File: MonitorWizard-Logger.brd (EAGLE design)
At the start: 120 x 80 mm, 28 parts, among them SW1 ACTION, U1 DHT22, U2 RFM69HW, U3 LTC3531, U4-NRF24L01 NRF24L01+-PCB-AERIAL, U6 ATMEGA328P-PU, X3 POWERSUPPLY_DC21MMX, Y3 32.768kHz

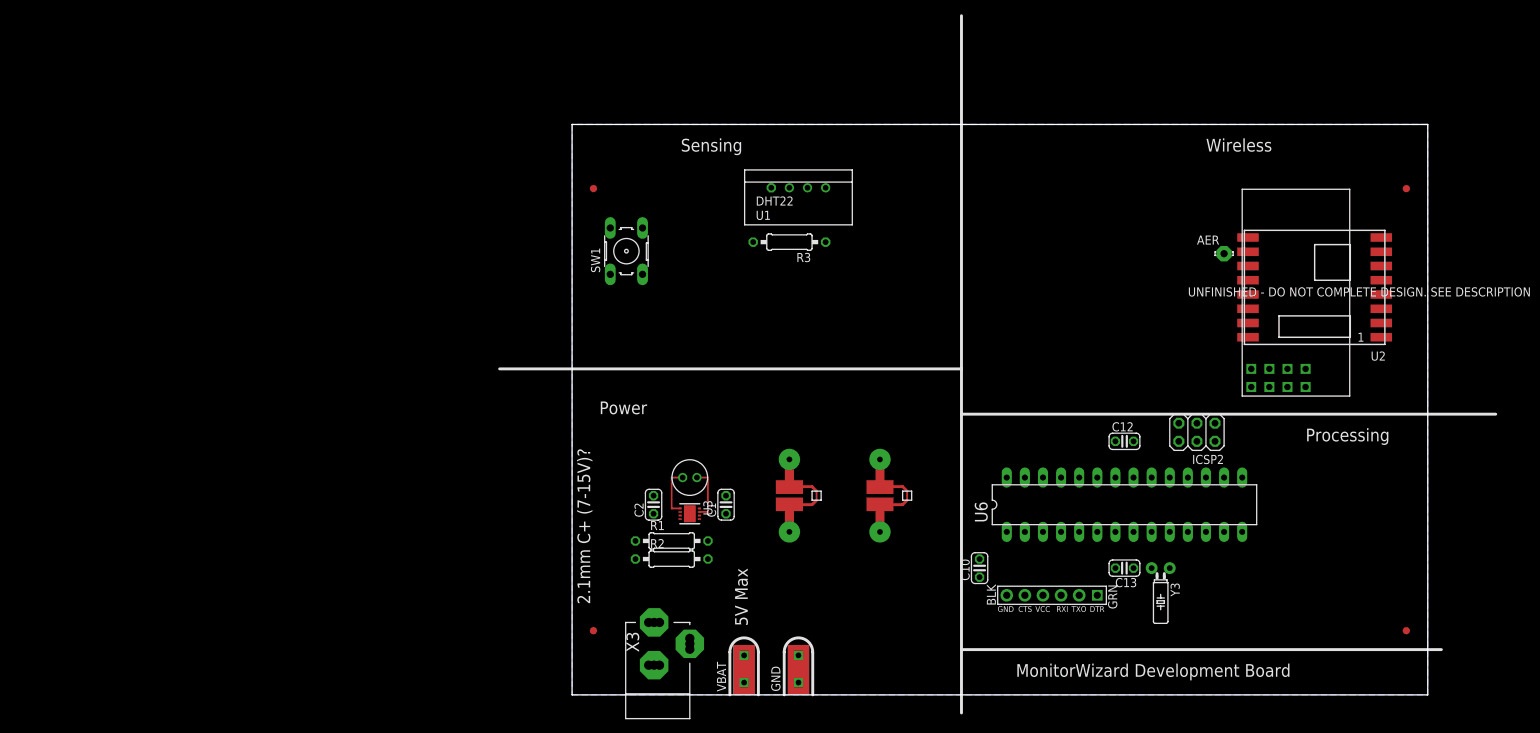
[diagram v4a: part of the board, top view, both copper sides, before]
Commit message: Add SD card, battery box. Nearly finished - just have to connect SD and lay out.
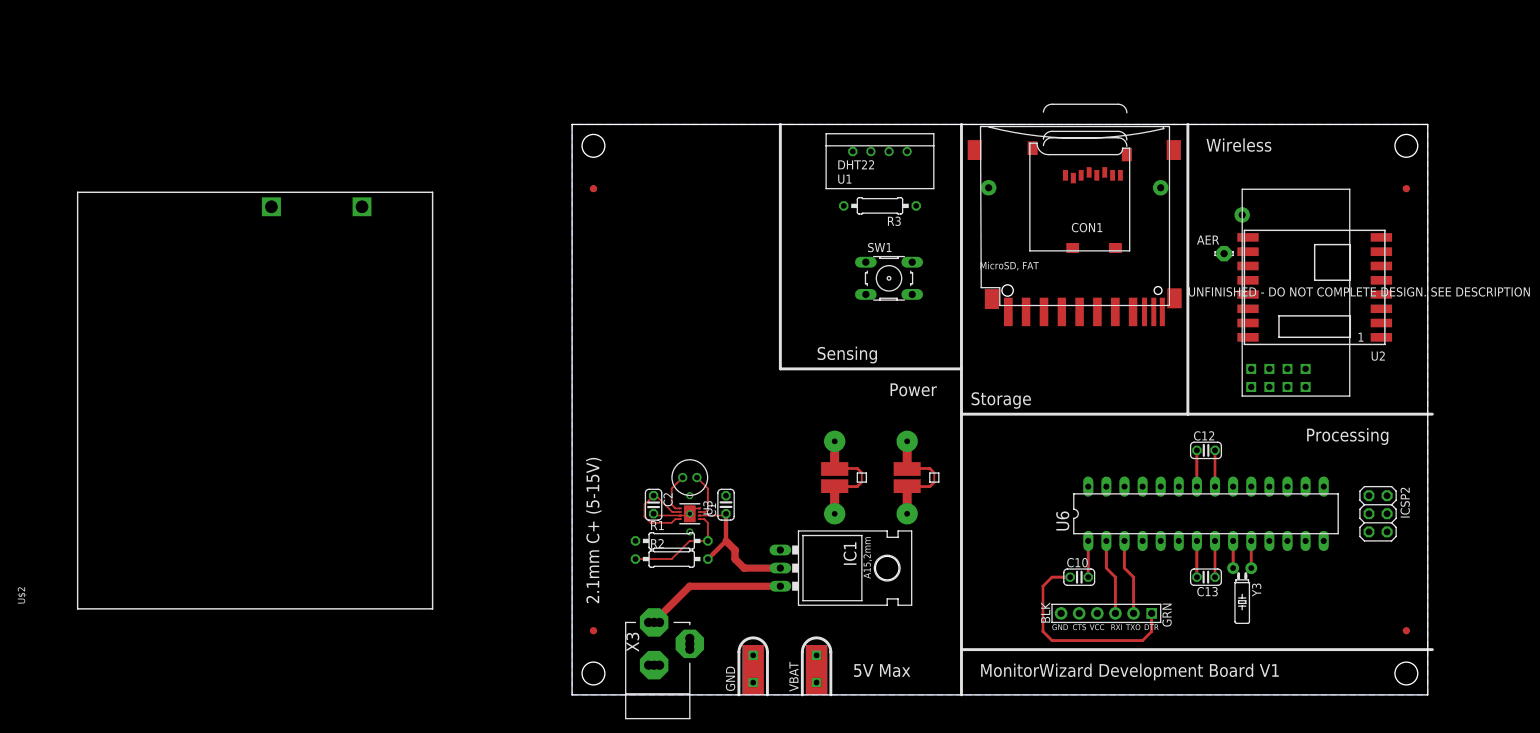
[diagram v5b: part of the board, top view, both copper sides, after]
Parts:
- added CON1: MICROSD, adafruit:MICROSD
- added IC1: LD117AV33, v-reg:TO220L1
- added U$1: SDMMC06132, adafruit:06132
- added U$2: 2464, keystone:2464
- moved SW1 37.0 mm to (44.5, 58.4), turned to 0 degrees
- moved ICSP2 27.9 mm to (113.0, 25.4), turned to 270 degrees
- moved C10 14.0 mm to (71.1, 16.5), turned to 0 degrees
- moved R3 13.7 mm to (43.2, 68.6)
- moved U1 12.5 mm to (43.2, 76.2)
- moved C12 11.5 mm to (88.9, 34.3)
- moved C13 11.5 mm to (88.9, 16.5)
- moved U6 11.5 mm to (88.9, 25.4)
- moved Y3 11.4 mm to (94.0, 17.8)
- moved VBAT 10.2 mm to (34.3, 0.00)
- moved JP1 8.03 mm to (74.9, 11.4)
- moved SENSOR_CURRENT 6.84 mm to (36.8, 30.5)
- moved GND 6.35 mm to (25.4, 0.00)
- moved RF_CURRENT 4.58 mm to (47.0, 30.5)
- turned C2 to 270 degrees
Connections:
- removed net VCC: C13.2, U6.20, U6.7
- new net SD_CS: CON1.2, U$1.1
- new net SD_DAT1: CON1.8, U$1.8
- new net SD_DAT2: CON1.1, U$1.9
- new net SD_DIN: CON1.3, U$1.2
- new net SD_DO: CON1.7, U$1.7
- new net SD_SCLK: CON1.5, U$1.5
- net 3V3: now also C13.2, CON1.4, IC1.2, U$1.4, U6.20, U6.7
- net GND: now also CON1.6, CON1.MT1, CON1.MT2, IC1.1, U$1.3, U$1.6, U$1.GP, U$2.-
- net VBAT: now also U$2.+
- net VBJ: now also IC1.3
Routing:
- net FTDI_DTR: track 0.00 -> 29.5 mm
- net 3V3: track 0.00 -> 26.4 mm
- net VBJ: track 0.00 -> 19.9 mm
- net GND: track 0.00 -> 17.3 mm, vias 0 -> 6
- net N$3: track 0.00 -> 15.2 mm
- net VBAT: track 0.00 -> 13.8 mm
- net 328_TXD: track 0.00 -> 10.7 mm
- net 328_RXD: track 0.00 -> 10.7 mm
- net RESET1: track 0.00 -> 5.08 mm
- net AREF: track 0.00 -> 5.08 mm
- net XTAL_P: track 0.00 -> 3.81 mm
- net XTAL_N: track 0.00 -> 3.81 mm
- net N$2: track 7.06 -> 5.85 mm
- net N$1: track 7.56 -> 6.45 mm
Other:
- board text added: "2.1mm C+ (5-15V)"
- board text added: "MicroSD, FAT"
- board text added: "MonitorWizard Development Board V1"
- board text added: "Storage"
- board text removed: "2.1mm C+ (7-15V)?"
- board text removed: "MonitorWizard Development Board"

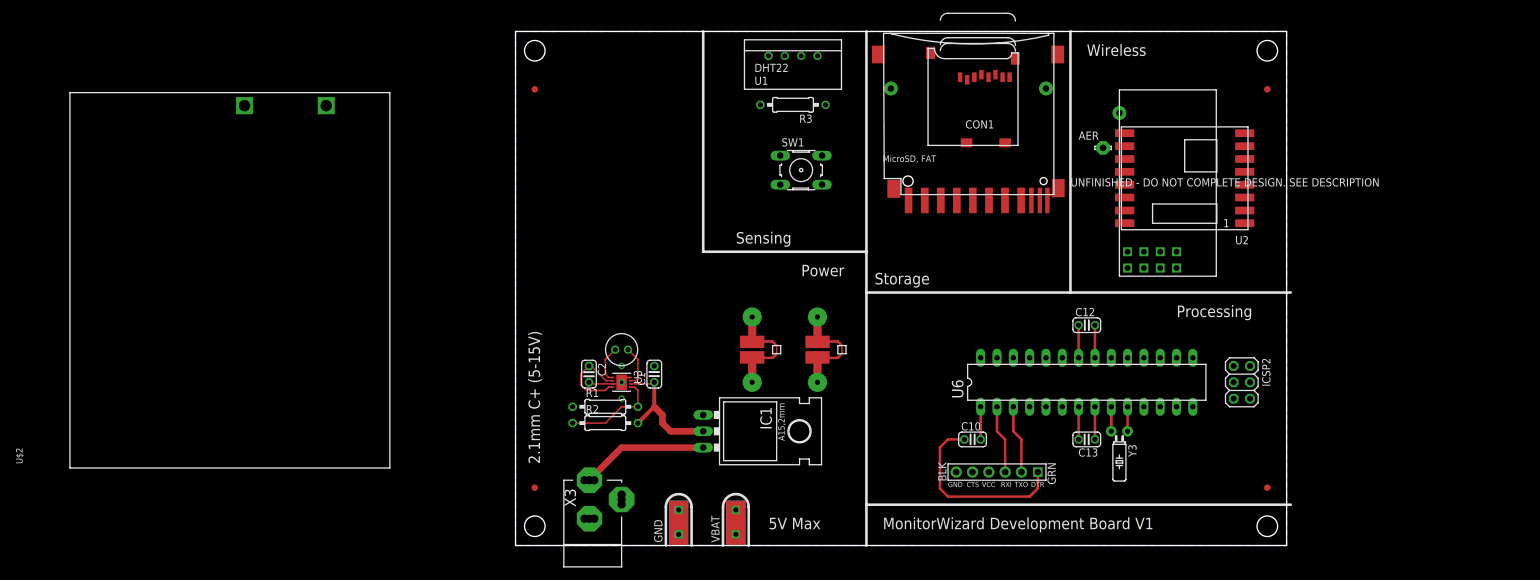
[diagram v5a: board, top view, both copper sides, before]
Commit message: Hopefully completed the schematic.
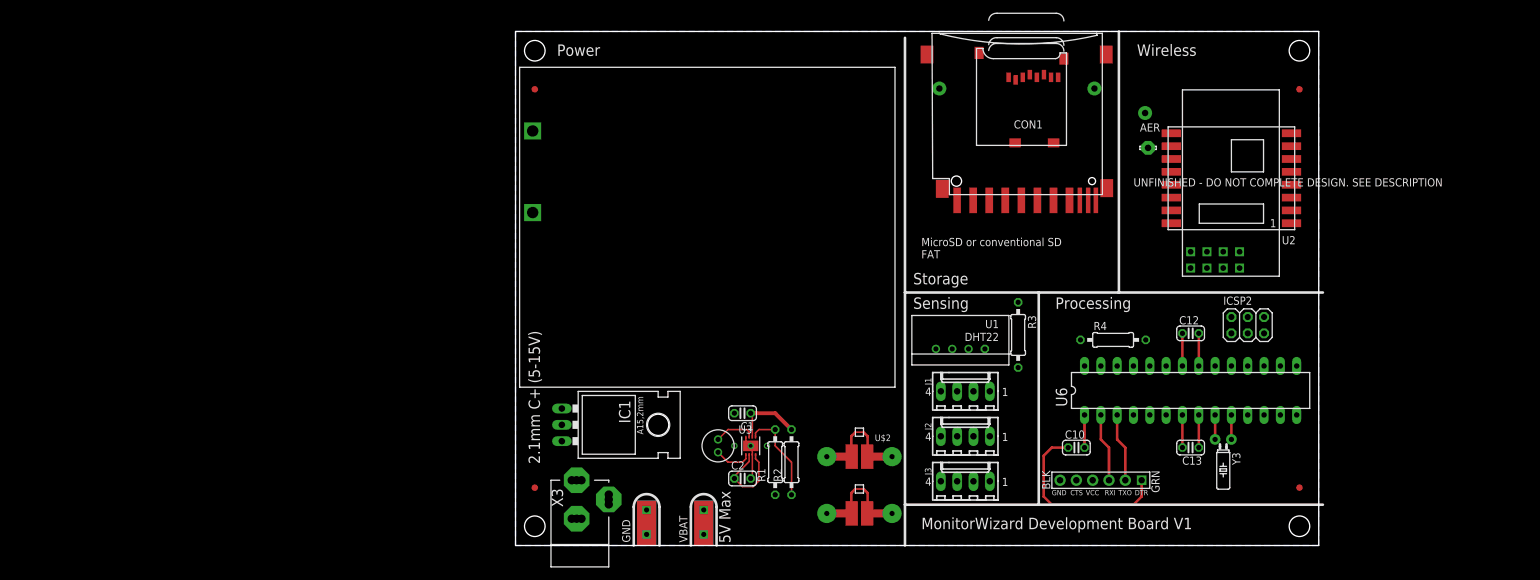
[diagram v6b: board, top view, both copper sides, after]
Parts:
- removed SW1: ACTION, switch-omron:B3F-10XX
- added J1, J2, J3: 22-27-2041-04, con-molex:6410-04
- added R4: TBD, resistor:0207/10
- moved U$2 75.5 mm to (30.5, 49.5), turned to 180 degrees
- moved U1 52.5 mm to (69.2, 30.6), turned to 180 degrees
- moved R3 50.1 mm to (78.2, 32.8), turned to 270 degrees
- moved R2 29.6 mm to (43.0, 13.0), turned to 90 degrees
- moved C2 28.9 mm to (35.3, 10.4), turned to 0 degrees
- moved R1 27.8 mm to (40.4, 13.0), turned to 90 degrees
- moved RF_CURRENT 26.3 mm to (53.5, 4.99), turned to 90 degrees
- moved SENSOR_CURRENT 23.6 mm to (53.5, 13.8), turned to 90 degrees
- moved U3 22.4 mm to (36.6, 15.5), turned to 0 degrees
- moved IC1 22.0 mm to (11.0, 18.8)
- moved L1 21.2 mm to (31.5, 15.5), turned to 90 degrees
- moved C10 16.2 mm to (87.3, 15.2)
- moved C12 16.2 mm to (105.1, 33.0)
- moved C13 16.2 mm to (105.1, 15.2)
- moved JP1 16.2 mm to (91.1, 10.2)
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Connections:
- net SENSOR_POWER renamed EXT_SENSOR_POWER
- removed net RFMODULE_MISO: U2.13, U4-NRF24L01.P$7
- removed net RFMODULE_MOSI: U2.14, U4-NRF24L01.P$6
- removed net RFMODULE_SCK: U2.12, U4-NRF24L01.P$5
- removed net RF_SS: U6.16
- removed net SD_DIN: CON1.3, U$1.2
- removed net SD_DO: CON1.7, U$1.7
- removed net SD_SCLK: CON1.5, U$1.5
- removed net SENSOR_3V3: R3.2, SENSOR_CURRENT.P$2, U1.VDD
- new net DHT22_3V3: R3.2, U1.VDD, U6.13
- new net EXT_ANALOG_0_TIM: J1.2, U6.11, U6.23
- new net EXT_ANALOG_1: J1.3, U6.24
- new net EXT_ANALOG_2: J2.2, U6.25
- new net EXT_ANALOG_3: J2.3, U6.26
- new net EXT_ANALOG_4: J3.2, U6.27
- new net EXT_ANALOG_5: J3.3, U6.28
- new net EXT_SENSOR_3V3: J1.1, J2.1, J3.1, R4.1, SENSOR_CURRENT.P$2
- new net RFMODULE_MISC2_INT: U2.2, U4-NRF24L01.P$8
- new net SD_DETECT: CON1.CD1, U$1.CD, U6.5
- net AREF: now also R4.2
- net DHT22_DATA: now also U6.6; no longer U6.23
- net GND: now also CON1.CD2, J1.4, J2.4, J3.4, U$1.GP3; no longer SW1.1, SW1.2
- net MISO1: now also CON1.7, U$1.7, U2.13, U4-NRF24L01.P$7
- net MOSI1: now also CON1.3, U$1.2, U2.14, U4-NRF24L01.P$6
- net RFMODULE_CS: now also U6.16
- net RFMODULE_MISC2: no longer U2.2, U4-NRF24L01.P$8
- net SCK1: now also CON1.5, U$1.5, U2.12, U4-NRF24L01.P$5
- net SD_CS: now also U6.14
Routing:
- net VBJ: track 19.9 -> 0.08 mm
- net 3V3: track 26.4 -> 16.5 mm
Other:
- board size 120 x 80 mm -> 125 x 80 mm
- board text added: "MicroSD or conventional SD FAT"
- board text removed: "MicroSD, FAT"

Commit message: Fiddle with layout slightly.
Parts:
- moved AER 25.5 mm to (121.6, 51.1), turned to 180 degrees
- moved U4-NRF24L01 24.2 mm to (111.1, 68.5), turned to 180 degrees
- moved U2 3.11 mm to (108.6, 55.9), turned to 0 degrees
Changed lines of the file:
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@@
 <element name="C12" library="rcl" package="C025-024X044" value="0.1u" x="105.06" y="33.02"/>
 <element name="C13" library="rcl" package="C025-024X044" value="0.1u" x="105.06" y="15.24" rot="R180"/>
-<element name="U4-NRF24L01" library="Radios" package="NRF24L01-PCB-AERIAL" value="NRF24L01+-PCB-AERIAL" x="108.87" y="44.45"/>
+<element name="U4-NRF24L01" library="Radios" package="NRF24L01-PCB-AERIAL" value="NRF24L01+-PCB-AERIAL" x="111.13" y="68.55" rot="R180"/>
 <element name="RF_CURRENT" library="Probes" package="CURRENT_MEASURE" value="CURRENT_MEASURE_0.4A" x="53.52" y="4.99" rot="R90"/>
 <element name="ICSP2" library="SmartPrj" package="2X03" value="3x2 M" x="113.95" y="34.29"/>
-<element name="AER" library="solpad" package="LSP10" value="LSP10" x="98.44" y="61.88" smashed="yes">
-<attribute name="NAME" x="97.17" y="64.42" size="1.27" layer="25" font="vector" ratio="10"/>
-<attribute name="VALUE" x="98.44" y="62.134" size="0.0254" layer="27"/>
+<element name="AER" library="solpad" package="LSP10" value="LSP10" x="121.56" y="51.12" smashed="yes" rot="R180">
+<attribute name="NAME" x="123.83" y="49.58" size="1.27" layer="25" font="vector" ratio="10" rot="R180"/>
+<attribute name="VALUE" x="121.56" y="50.866" size="0.0254" layer="27" rot="R180"/>
 </element>
 <element name="GND" library="Probes" package="ALLIGATOR" value="ALLIGATOR" x="20.4" y="0"/>
@@
 </element>
 <element name="R3" library="resistor" package="0207/10" value="10K" x="78.22" y="32.77" rot="R270"/>
-<element name="U2" library="SparkFun-RF" package="RFM69W-XXXS2" value="RFM69HW" x="111.41" y="57.15" rot="R180"/>
+<element name="U2" library="SparkFun-RF" package="RFM69W-XXXS2" value="RFM69HW" x="108.59" y="55.85"/>
 <element name="U3" library="linear-sen" package="DFN8-3X3" value="LTC3531" x="36.6" y="15.51"/>
 <element name="L1" library="InductorsThru" package="L-RADIAL-2-5OD" value="10uH" x="31.52" y="15.51" rot="R90"/>
@@
 <via x="65.96" y="71.12" extent="1-16" drill="1" diameter="2.1844"/>
 <via x="90.09" y="71.12" extent="1-16" drill="1" diameter="2.1844"/>
-<via x="97.98" y="67.31" extent="1-16" drill="1" diameter="2.1844"/>
+<via x="119.02" y="42.69" extent="1-16" drill="1" diameter="2.1844"/>
 <contactref element="U$2" pad="-"/>
 <contactref element="J1" pad="4"/>
@@
 <contactref element="CON1" pad="CD2"/>
 <contactref element="U$1" pad="GP3"/>
-<wire x1="90.09" y1="71.12" x2="91.92" y2="76.41" width="0" layer="19" extent="1-1"/>
+<wire x1="117.94" y1="48.85" x2="117.94" y2="52.85" width="0" layer="19" extent="1-1"/>
+<wire x1="119.02" y1="42.69" x2="117.94" y2="48.85" width="0" layer="19" extent="1-1"/>
 <wire x1="20.4" y1="3.5" x2="20.4" y2="3.5" width="0" layer="19" extent="1-16"/>
-<wire x1="102.06" y1="64.15" x2="97.98" y2="67.31" width="0" layer="19" extent="1-1"/>
-<wire x1="102.06" y1="60.15" x2="102.06" y2="64.15" width="0" layer="19" extent="1-1"/>
+<wire x1="91.92" y1="76.41" x2="90.09" y2="71.12" width="0" layer="19" extent="1-1"/>
 <wire x1="85.34" y1="75.77" x2="91.92" y2="76.41" width="0" layer="19" extent="1-1"/>
 <wire x1="82.24" y1="73.27" x2="85.34" y2="75.77" width="0" layer="19" extent="1-1"/>
-<wire x1="66.19" y1="24" x2="65.42" y2="30.6" width="0" layer="19" extent="1-1"/>
-<wire x1="66.19" y1="17" x2="66.19" y2="24" width="0" layer="19" extent="1-1"/>
-<wire x1="66.19" y1="10" x2="66.19" y2="17" width="0" layer="19" extent="1-1"/>
 <wire x1="72.14" y1="76.67" x2="65.96" y2="71.12" width="0" layer="19" extent="1-1"/>
 <wire x1="77.74" y1="62.67" x2="82.24" y2="73.27" width="0" layer="19" extent="1-1"/>
@@
 <wire x1="106.33" y1="33.02" x2="106.33" y2="27.94" width="0.4064" layer="1"/>
 <contactref element="R4" pad="2"/>
-<wire x1="98.08" y1="32" x2="106.33" y2="27.94" width="0" layer="19" extent="1-1"/>
+<wire x1="98.08" y1="32" x2="106.33" y2="33.02" width="0" layer="19" extent="1-1"/>
 </signal>
 <signal name="328_TXD">
@@
 <contactref element="U$1" pad="5"/>
 <contactref element="CON1" pad="5"/>
-<wire x1="110.14" y1="43.18" x2="102.06" y2="58.15" width="0" layer="19" extent="1-1"/>
-<wire x1="113.95" y1="33.02" x2="110.14" y2="43.18" width="0" layer="19" extent="1-1"/>
+<wire x1="117.94" y1="54.85" x2="109.86" y2="69.82" width="0" layer="19" extent="1-1"/>
+<wire x1="113.95" y1="33.02" x2="117.94" y2="54.85" width="0" layer="19" extent="1-1"/>
 <wire x1="111.41" y1="27.94" x2="113.95" y2="33.02" width="0" layer="19" extent="1-1"/>
-<wire x1="81.22" y1="53.71" x2="102.06" y2="58.15" width="0" layer="19" extent="1-1"/>
-<wire x1="81.14" y1="72.87" x2="81.22" y2="53.71" width="0" layer="19" extent="1-1"/>
+<wire x1="81.14" y1="72.87" x2="109.86" y2="69.82" width="0" layer="19" extent="1-1"/>
+<wire x1="81.22" y1="53.71" x2="81.14" y2="72.87" width="0" layer="19" extent="1-1"/>
 </signal>
 <signal name="MISO1">
@@
 <contactref element="U$1" pad="7"/>
 <contactref element="CON1" pad="7"/>
-<wire x1="86.22" y1="53.71" x2="102.06" y2="56.15" width="0" layer="19" extent="1-1"/>
-<wire x1="112.68" y1="43.18" x2="102.06" y2="56.15" width="0" layer="19" extent="1-1"/>
-<wire x1="111.41" y1="33.02" x2="112.68" y2="43.18" width="0" layer="19" extent="1-1"/>
+<wire x1="117.94" y1="56.85" x2="107.32" y2="69.82" width="0" layer="19" extent="1-1"/>
+<wire x1="83.34" y1="72.87" x2="107.32" y2="69.82" width="0" layer="19" extent="1-1"/>
+<wire x1="86.22" y1="53.71" x2="83.34" y2="72.87" width="0" layer="19" extent="1-1"/>
+<wire x1="111.41" y1="33.02" x2="117.94" y2="56.85" width="0" layer="19" extent="1-1"/>
 <wire x1="113.95" y1="27.94" x2="111.41" y2="33.02" width="0" layer="19" extent="1-1"/>
-<wire x1="83.34" y1="72.87" x2="86.22" y2="53.71" width="0" layer="19" extent="1-1"/>
 </signal>
 <signal name="RFMODULE_3V3">
@@
 <contactref element="RF_CURRENT" pad="P$2"/>
 <contactref element="U2" pad="8"/>
-<wire x1="105.06" y1="45.72" x2="120.76" y2="64.15" width="0" layer="19" extent="1-1"/>
-<wire x1="58.6" y1="4.99" x2="105.06" y2="45.72" width="0" layer="19" extent="1-1"/>
+<wire x1="99.24" y1="48.85" x2="114.94" y2="67.28" width="0" layer="19" extent="1-1"/>
+<wire x1="58.6" y1="4.99" x2="99.24" y2="48.85" width="0" layer="19" extent="1-1"/>
 </signal>
 <signal name="N$9">
 <contactref element="AER" pad="MP"/>
 <contactref element="U2" pad="10"/>
-<wire x1="98.44" y1="61.88" x2="102.06" y2="62.15" width="0" layer="19" extent="1-1"/>
+<wire x1="117.94" y1="50.85" x2="121.56" y2="51.12" width="0" layer="19" extent="1-1"/>
 </signal>
 <signal name="RFMODULE_MISC1">
@@
 <contactref element="U2" pad="1"/>
 <contactref element="U6" pad="12"/>
-<wire x1="107.6" y1="43.18" x2="120.76" y2="50.15" width="0" layer="19" extent="1-1"/>
-<wire x1="116.49" y1="20.32" x2="107.6" y2="43.18" width="0" layer="19" extent="1-1"/>
+<wire x1="99.24" y1="62.85" x2="112.4" y2="69.82" width="0" layer="19" extent="1-1"/>
+<wire x1="116.49" y1="20.32" x2="99.24" y2="62.85" width="0" layer="19" extent="1-1"/>
 </signal>
 <signal name="RFMODULE_MISC2">
@@
 <contactref element="U4-NRF24L01" pad="P$8"/>
 <contactref element="U2" pad="2"/>
-<wire x1="112.68" y1="45.72" x2="120.76" y2="52.15" width="0" layer="19" extent="1-1"/>
+<wire x1="99.24" y1="60.85" x2="107.32" y2="67.28" width="0" layer="19" extent="1-1"/>
 </signal>
 <signal name="RFMODULE_CS">
@@
 <contactref element="U4-NRF24L01" pad="P$4"/>
 <contactref element="U2" pad="15"/>
-<wire x1="102.06" y1="52.15" x2="107.6" y2="45.72" width="0" layer="19" extent="1-1"/>
-<wire x1="119.03" y1="27.94" x2="107.6" y2="45.72" width="0" layer="19" extent="1-1"/>
+<wire x1="117.94" y1="60.85" x2="112.4" y2="67.28" width="0" layer="19" extent="1-1"/>
+<wire x1="119.03" y1="27.94" x2="117.94" y2="60.85" width="0" layer="19" extent="1-1"/>
 </signal>
 <signal name="MOSI1">
@@
 <contactref element="U4-NRF24L01" pad="P$6"/>
 <contactref element="U2" pad="14"/>
-<wire x1="113.95" y1="35.56" x2="110.14" y2="45.72" width="0" layer="19" extent="1-1"/>
+<wire x1="117.94" y1="58.85" x2="109.86" y2="67.28" width="0" layer="19" extent="1-1"/>
+<wire x1="113.95" y1="35.56" x2="117.94" y2="58.85" width="0" layer="19" extent="1-1"/>
 <wire x1="116.49" y1="27.94" x2="113.95" y2="35.56" width="0" layer="19" extent="1-1"/>
-<wire x1="102.06" y1="54.15" x2="110.14" y2="45.72" width="0" layer="19" extent="1-1"/>
-<wire x1="73.72" y1="53.71" x2="102.06" y2="54.15" width="0" layer="19" extent="1-1"/>
-<wire x1="78.94" y1="72.87" x2="73.72" y2="53.71" width="0" layer="19" extent="1-1"/>
+<wire x1="78.94" y1="72.87" x2="109.86" y2="67.28" width="0" layer="19" extent="1-1"/>
+<wire x1="73.72" y1="53.71" x2="78.94" y2="72.87" width="0" layer="19" extent="1-1"/>
 </signal>
 <signal name="EXT_ANALOG_4">
@@
 <contactref element="R4" pad="1"/>
 <contactref element="SENSOR_CURRENT" pad="P$2"/>
+<wire x1="73.81" y1="24" x2="87.92" y2="32" width="0" layer="19" extent="1-1"/>
 <wire x1="73.81" y1="17" x2="73.81" y2="24" width="0" layer="19" extent="1-1"/>
 <wire x1="73.81" y1="10" x2="73.81" y2="17" width="0" layer="19" extent="1-1"/>
 <wire x1="58.6" y1="13.83" x2="73.81" y2="17" width="0" layer="19" extent="1-1"/>
-<wire x1="87.92" y1="32" x2="54.79" y2="13.83" width="0" layer="19" extent="1-1"/>
 </signal>
 </signals>

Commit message: Update battery box footprint.
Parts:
- moved J1 2.24 mm to (68.0, 25.0), turned to 180 degrees
- moved J2 2.00 mm to (68.0, 17.0), turned to 180 degrees
- moved J3 2.00 mm to (68.0, 10.0), turned to 180 degrees
- moved U$2 0.50 mm to (30.0, 49.5)
- moved U1 0.50 mm to (69.2, 31.1)
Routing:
- net 3V3: track 16.5 -> 50.5 mm
- net VBJ: track 0.08 -> 7.03 mm
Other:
- board text added: "Not heatsinked - current draw should not be significant enough to warrant heatsinking, even at higher voltage inputs."
- board text added: "Pins (1-4): 3V3, A1, A2, GND"
